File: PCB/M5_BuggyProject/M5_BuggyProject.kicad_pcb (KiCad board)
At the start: 2 copper layers, 9 parts, among them J1 XT60

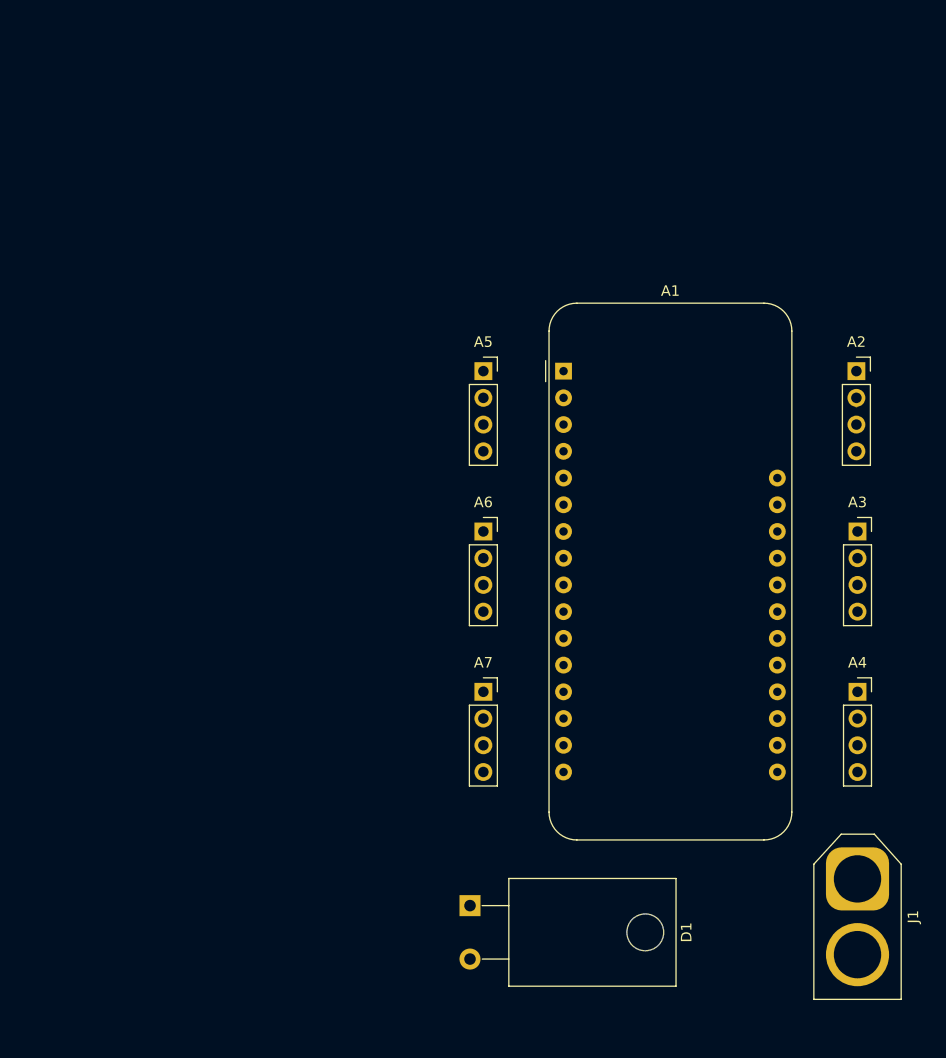
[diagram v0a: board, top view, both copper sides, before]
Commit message: Edited title blocks, netlist
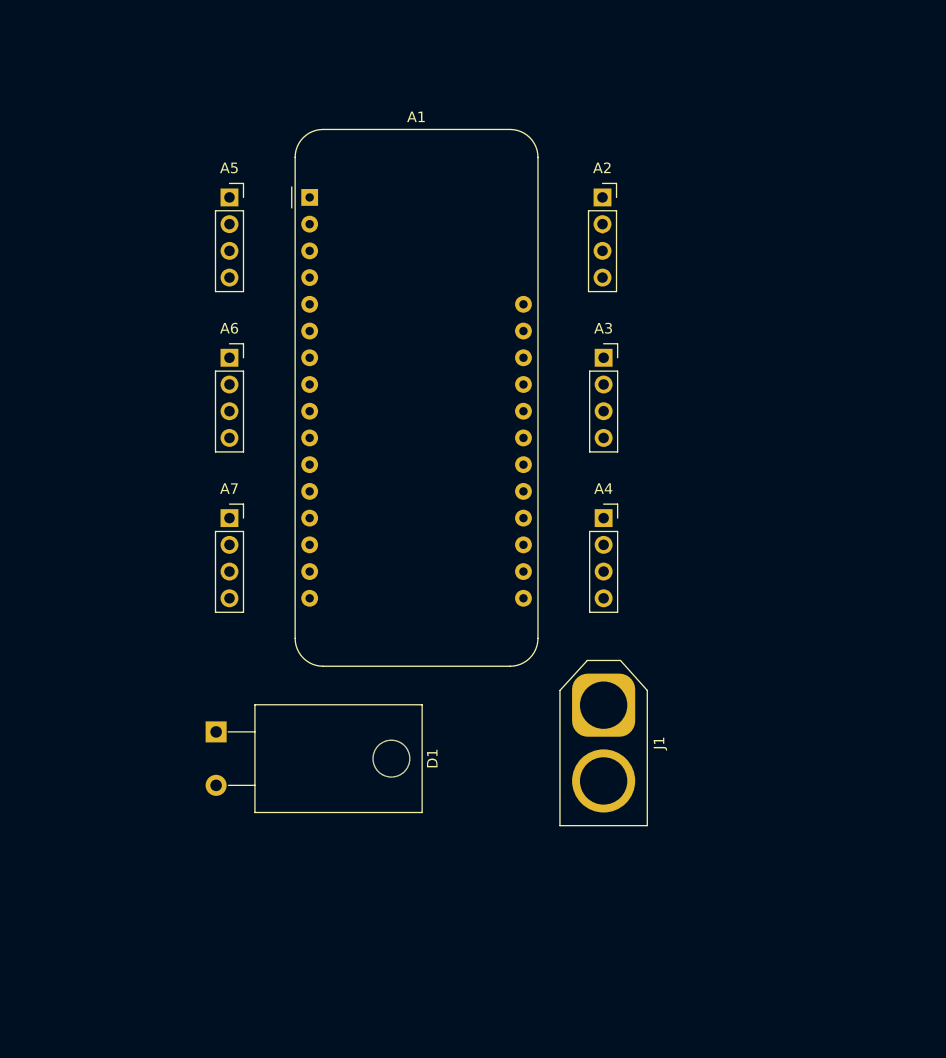
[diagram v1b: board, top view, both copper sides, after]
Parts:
- moved A1 29.2 mm to (101.6, 47.0)
- moved A4 29.2 mm to (129.5, 77.5)
- moved A7 29.2 mm to (94.0, 77.5)
- moved D1 29.2 mm to (92.7, 97.8)
- moved J1 29.2 mm to (129.5, 95.2)
- moved A2 29.2 mm to (129.4, 47.0)
- moved A3 29.2 mm to (129.5, 62.2)
- moved A5 29.2 mm to (94.0, 47.0)
- moved A6 29.2 mm to (94.0, 62.2)
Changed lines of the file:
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@@
     (nets 31)
   )
-  (page A4)
+  (page User 215.9 177.8)
   (title_block
     (title "All-Terrain Buggy")
@@
     (rev v1.0)
     (company "M5 Makerspace")
-    (comment 3 "CC BY 4.0")
+    (comment 2 creativecommons.org/licenses/by/4.0/)
+    (comment 3 "License: CC BY 4.0")
     (comment 4 "Authors: Akshat Sahay, Sebastian Armstrong")
   )
@@
   )
   (module Connector_PinSocket_2.54mm:PinSocket_1x04_P2.54mm_Vertical (layer F.Cu)
-    (at 153.67 93.98)
+    (at 129.54 77.47)
     (descr "Through hole straight socket strip, 1x04, 2.54mm pitch, single row (from Kicad 4.0.7), script generated")
     (tags "Through hole socket strip THT 1x04 2.54mm single row")
@@
   )
   (module Module:Adafruit_Feather (layer F.Cu)
-    (at 125.73 63.5)
+    (at 101.6 46.99)
     (descr "Common footprint for the Adafruit Feather series of boards, https://learn.adafruit.com/adafruit-feather/feather-specification")
     (tags "Adafruit Feather")
@@
   )
   (module Connector_PinSocket_2.54mm:PinSocket_1x04_P2.54mm_Vertical (layer F.Cu)
-    (at 153.565001 63.5)
+    (at 129.435001 46.99)
     (descr "Through hole straight socket strip, 1x04, 2.54mm pitch, single row (from Kicad 4.0.7), script generated")
     (tags "Through hole socket strip THT 1x04 2.54mm single row")
@@
   )
   (module Connector_PinSocket_2.54mm:PinSocket_1x04_P2.54mm_Vertical (layer F.Cu)
-    (at 153.67 78.74)
+    (at 129.54 62.23)
     (descr "Through hole straight socket strip, 1x04, 2.54mm pitch, single row (from Kicad 4.0.7), script generated")
     (tags "Through hole socket strip THT 1x04 2.54mm single row")
@@
   )
   (module Connector_PinSocket_2.54mm:PinSocket_1x04_P2.54mm_Vertical (layer F.Cu)
-    (at 118.11 63.5)
+    (at 93.98 46.99)
     (descr "Through hole straight socket strip, 1x04, 2.54mm pitch, single row (from Kicad 4.0.7), script generated")
     (tags "Through hole socket strip THT 1x04 2.54mm single row")
@@
   )
   (module Connector_PinSocket_2.54mm:PinSocket_1x04_P2.54mm_Vertical (layer F.Cu)
-    (at 118.11 78.74)
+    (at 93.98 62.23)
     (descr "Through hole straight socket strip, 1x04, 2.54mm pitch, single row (from Kicad 4.0.7), script generated")
     (tags "Through hole socket strip THT 1x04 2.54mm single row")
@@
   )
   (module Connector_PinSocket_2.54mm:PinSocket_1x04_P2.54mm_Vertical (layer F.Cu)
-    (at 118.11 93.98)
+    (at 93.98 77.47)
     (descr "Through hole straight socket strip, 1x04, 2.54mm pitch, single row (from Kicad 4.0.7), script generated")
     (tags "Through hole socket strip THT 1x04 2.54mm single row")
@@
   )
   (module Package_TO_SOT_THT:TO-220-2_Horizontal_TabDown (layer F.Cu)
-    (at 116.84 114.3 270)
+    (at 92.71 97.79 270)
     (descr "TO-220-2, Horizontal, RM 5.08mm, see https://www.centralsemi.com/PDFS/CASE/TO-220-2PD.PDF")
     (tags "TO-220-2 Horizontal RM 5.08mm")
@@
   )
   (module Connector_AMASS:AMASS_XT60-F_1x02_P7.20mm_Vertical (layer F.Cu)
-    (at 153.67 111.76 270)
+    (at 129.54 95.25 270)
     (descr "AMASS female XT60, through hole, vertical, https://www.tme.eu/Document/2d152ced3b7a446066e6c419d84bb460/XT60%20SPEC.pdf")
     (tags "XT60 female vertical")
@@
     )
   )
-  (segment (start 153.565001 66.840998) (end 153.565001 66.04) (width 0.25) (layer F.Cu) (net 25))
+  (segment (start 129.435001 50.330998) (end 129.435001 49.53) (width 0.25) (layer F.Cu) (net 25))
 )

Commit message: Added labels, traces for controls
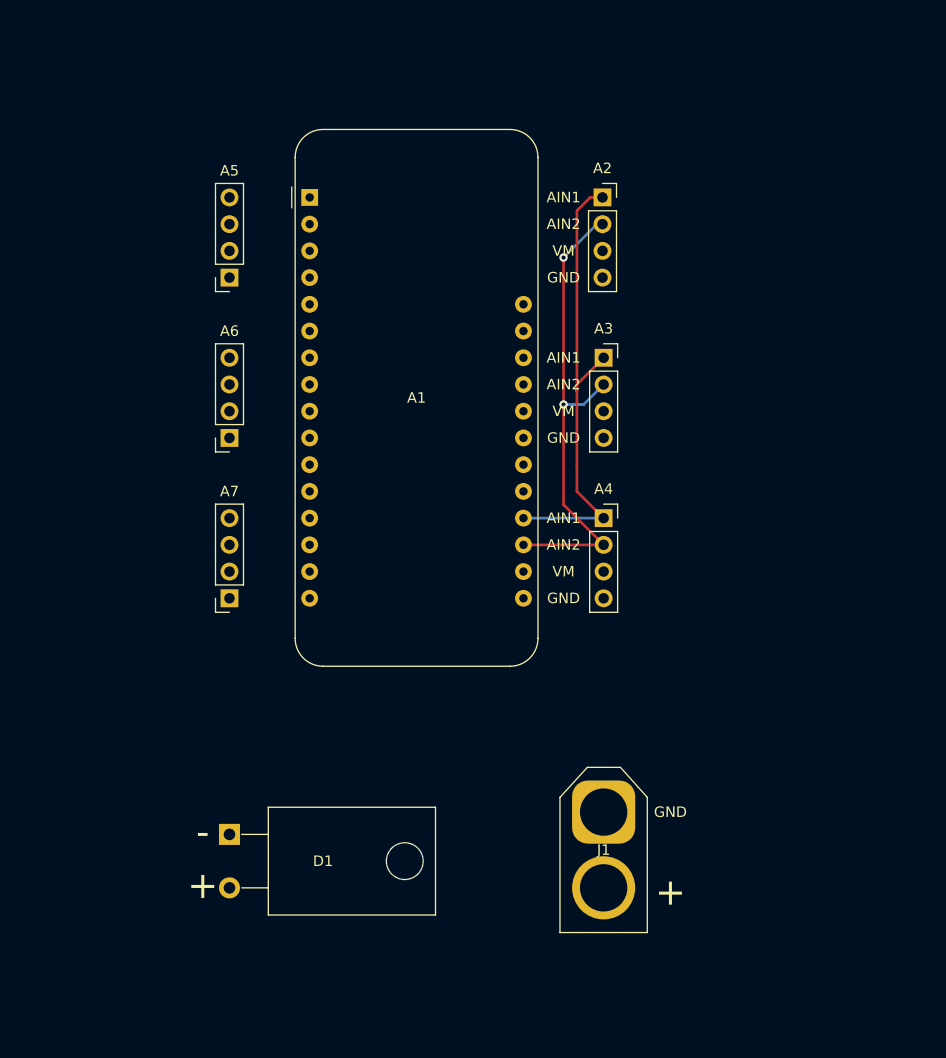
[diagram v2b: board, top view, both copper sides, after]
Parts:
- moved J1 10.2 mm to (129.5, 105.4)
- moved D1 9.82 mm to (94.0, 107.5)
- moved A7 7.62 mm to (94.0, 85.1), turned to 180 degrees
- moved A5 7.62 mm to (94.0, 54.6), turned to 180 degrees
- moved A6 7.62 mm to (94.0, 69.8), turned to 180 degrees
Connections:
- A1 pad 19: AIN1 -> AIN2
- A1 pad 20: AIN2 -> AIN1
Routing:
- net AIN2: track 0.80 -> 46.9 mm, vias 0 -> 2
- net AIN1: track 0.00 -> 45.7 mm
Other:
- net class Default: trace_width 0.25 -> 0.254
- board text added: "+"
- board text added: "-"
- board text added: "AIN1"
- board text added: "AIN2"
- board text added: "GND"
- board text added: "VM"

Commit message: Updated PCB, added Digikey footprint library
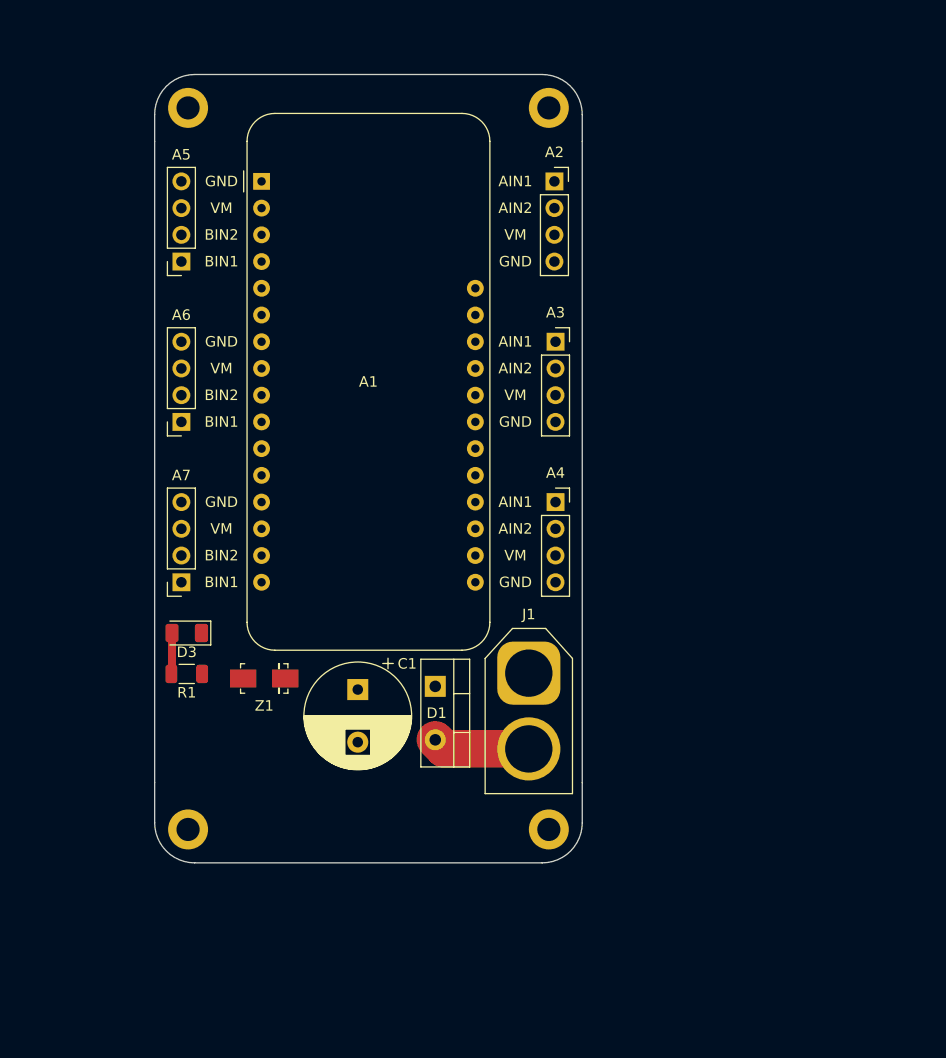
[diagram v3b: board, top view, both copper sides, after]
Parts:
- added C1: 2200uF, Capacitor_THT:CP_Radial_D10.0mm_P5.00mm, F.Cu at (106.2, 93.8)
- added D3: LED, LED_SMD:LED_1206_3216Metric, F.Cu at (89.9, 88.4)
- added M3: MountingHole_2.2mm_M2_DIN965_Pad, MountingHole:MountingHole_2.2mm_M2_DIN965_Pad, F.Cu at (90.0, 107.1)
- added M4: MountingHole_2.2mm_M2_DIN965_Pad, MountingHole:MountingHole_2.2mm_M2_DIN965_Pad, F.Cu at (124.3, 107.1)
- added R1: 698, Resistor_SMD:R_1206_3216Metric, F.Cu at (89.9, 92.3)
- added REF**: MountingHole_2.2mm_M2_DIN965_Pad, MountingHole:MountingHole_2.2mm_M2_DIN965_Pad, F.Cu at (124.3, 38.5)
- added REF**: MountingHole_2.2mm_M2_DIN965_Pad, MountingHole:MountingHole_2.2mm_M2_DIN965_Pad, F.Cu at (90.0, 38.5)
- added Z1: Diode, digikey-footprints:DO-214AC, F.Cu at (97.3, 92.7)
- D1: footprint Package_TO_SOT_THT:TO-220-2_Horizontal_TabDown -> Package_TO_SOT_THT:TO-220-2_Vertical
- J1: footprint Connector_AMASS:AMASS_XT60-F_1x02_P7.20mm_Vertical -> Connector_AMASS:AMASS_XT60-M_1x02_P7.20mm_Vertical
- moved D1 24.1 mm to (113.5, 93.5)
- moved J1 15.0 mm to (122.4, 92.2)
- moved A2 4.82 mm to (124.9, 45.5)
- moved A5 4.82 mm to (89.4, 53.1)
- moved A6 4.82 mm to (89.4, 68.3)
- moved A7 4.82 mm to (89.4, 83.6)
- moved A1 4.82 mm to (97.0, 45.5)
- moved A4 4.82 mm to (125.0, 75.9)
- moved A3 4.82 mm to (125.0, 60.7)
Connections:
- net +7.5V renamed +12V
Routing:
- net AIN2: track 46.9 -> 0.53 mm, vias 2 -> 0
- net AIN1: track 45.7 -> 0.63 mm
- net VCC: track 0.00 -> 9.25 mm
- net Net-(D3-Pad2): track 0.00 -> 3.91 mm
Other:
- board outline added: 40.6 x 74.9 mm
- board text added: "BIN1"
- board text added: "BIN2"
- board text removed: "+"
- board text removed: "-"

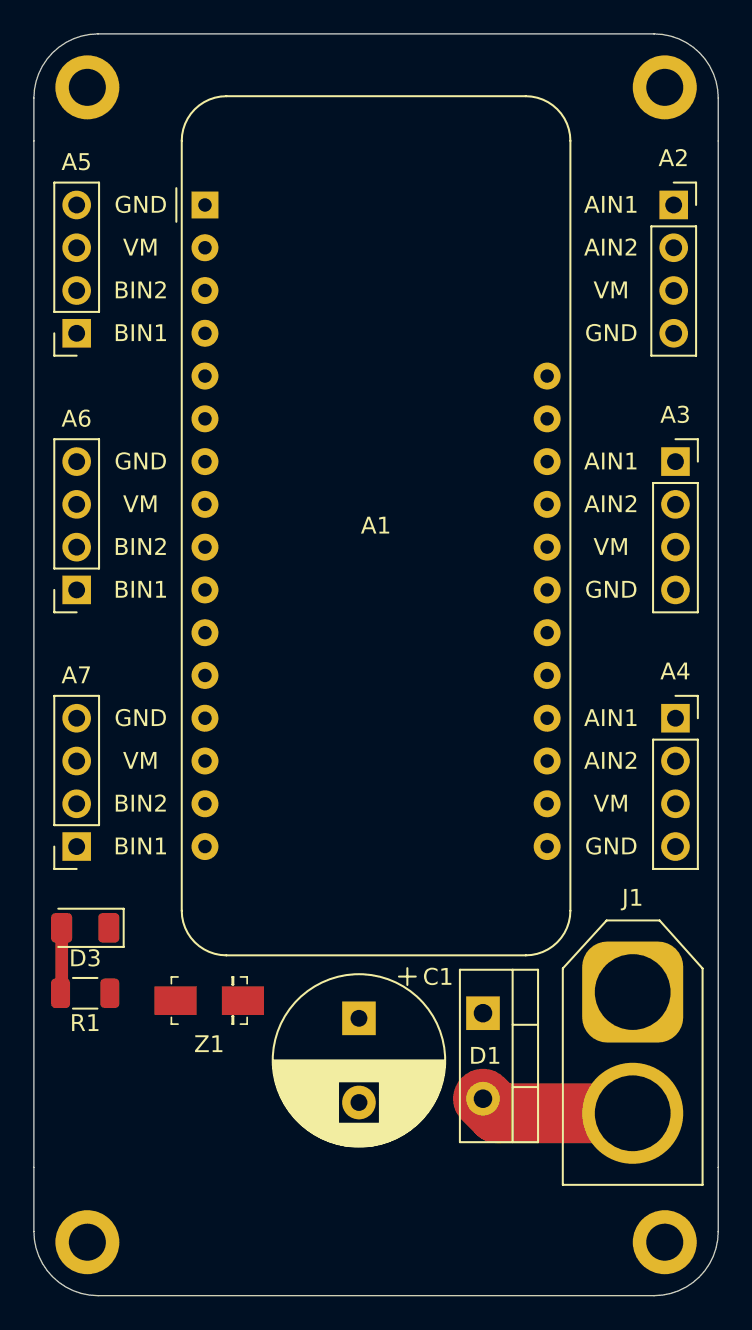
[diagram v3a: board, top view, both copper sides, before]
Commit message: Added graphics to PCB
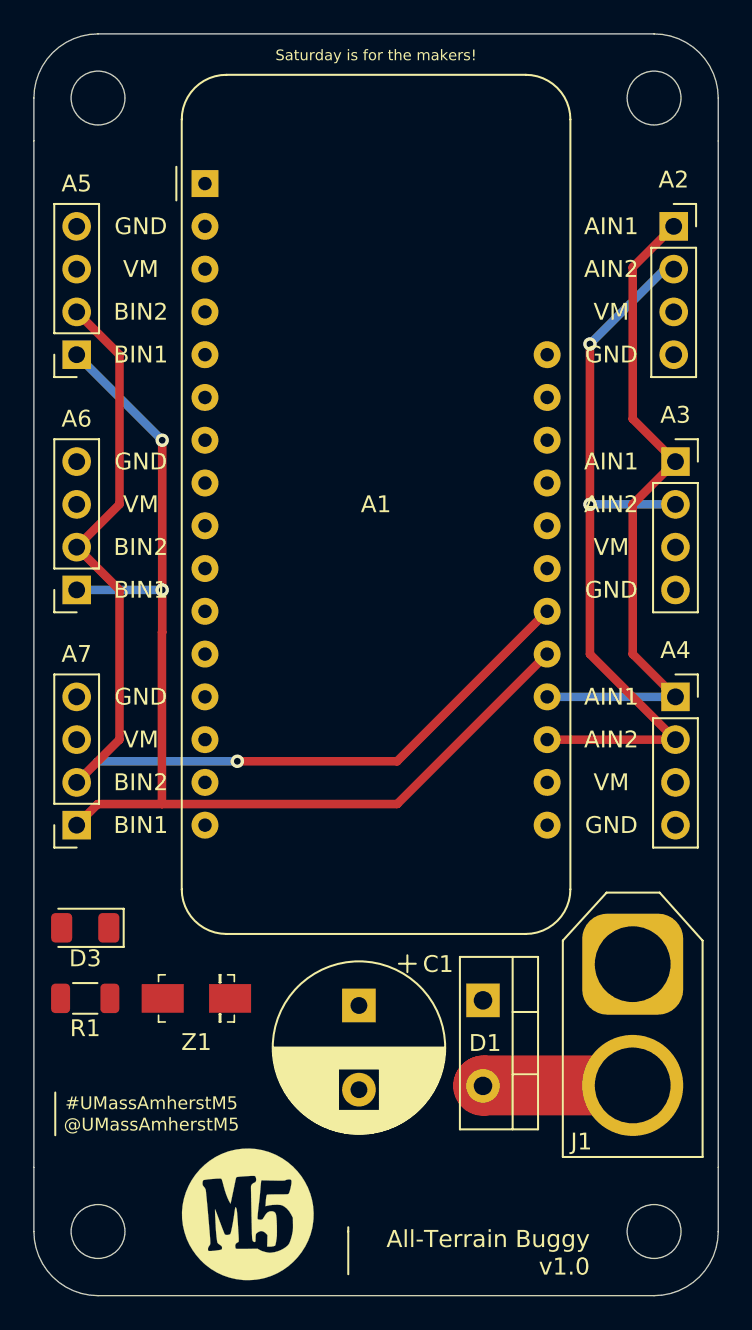
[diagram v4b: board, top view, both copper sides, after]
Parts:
- removed M3, M4: MountingHole_2.2mm_M2_DIN965_Pad, MountingHole:MountingHole_2.2mm_M2_DIN965_Pad
- removed the REF** at (124.3, 38.5)
- removed the REF** at (90.0, 38.5)
- added G***: LOGO, Figures:M5_logo, F.Cu at (99.6, 105.4)
- added REF**: MountingHole_3.2mm_M3, MountingHole:MountingHole_3.2mm_M3, F.Cu at (123.7, 39.1)
- added REF**: MountingHole_3.2mm_M3, MountingHole:MountingHole_3.2mm_M3, F.Cu at (90.7, 39.1)
- added REF**: MountingHole_3.2mm_M3, MountingHole:MountingHole_3.2mm_M3, F.Cu at (123.7, 106.4)
- added REF**: MountingHole_3.2mm_M3, MountingHole:MountingHole_3.2mm_M3, F.Cu at (90.7, 106.4)
- moved J1 1.66 mm to (122.4, 90.6)
- moved A1 1.27 mm to (97.0, 44.2)
- moved A5 1.27 mm to (89.4, 54.4)
- moved A2 1.27 mm to (124.9, 46.7)
- moved A4 1.27 mm to (125.0, 74.7)
- moved A7 1.27 mm to (89.4, 82.3)
- moved Z1 0.77 mm to (96.5, 92.6)
- moved C1 0.76 mm to (106.2, 93.0)
- moved D1 0.76 mm to (113.5, 92.7)
- moved R1 0.30 mm to (89.9, 92.6)
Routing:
- net BIN1: track 0.00 -> 66.0 mm, vias 0 -> 2
- net BIN2: track 0.25 -> 64.3 mm, vias 0 -> 1
- net AIN2: track 0.53 -> 45.1 mm, vias 0 -> 2
- net AIN1: track 0.63 -> 39.7 mm
- net Net-(D3-Pad2): track 3.91 -> 0.00 mm
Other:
- board text added: "#UMassAmherstM5"
- board text added: "@UMassAmherstM5"
- board text added: "All-Terrain Buggy v1.0"
- board text added: "Saturday is for the makers!"

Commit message: Finalised PCB for v1.0
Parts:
- removed REF** (x4): MountingHole_3.2mm_M3, MountingHole:MountingHole_3.2mm_M3
- added BZ1: BEEP, Buzzer_Beeper:Buzzer_12x9.5RM7.6, F.Cu at (107.2, 44.2)
- added D2: ORANGE, LED_SMD:LED_1206_3216Metric, F.Cu at (89.4, 45.5)
- added D4: ORANGE, LED_SMD:LED_1206_3216Metric, F.Cu at (93.2, 45.5)
- added H1: M, MountingHole:MountingHole_3.2mm_M3_Pad_Via, F.Cu at (80.5, 39.1)
- added H2: M, MountingHole:MountingHole_3.2mm_M3_Pad_Via, F.Cu at (113.5, 39.1)
- added H3: M, MountingHole:MountingHole_3.2mm_M3_Pad_Via, F.Cu at (113.5, 121.7)
- added H4: M, MountingHole:MountingHole_3.2mm_M3_Pad_Via, F.Cu at (80.5, 121.7)
- added J2: VCC, TestPoint:TestPoint_Loop_D1.80mm_Drill1.0mm_Beaded, F.Cu at (103.4, 117.9)
- added J3: 10V, TestPoint:TestPoint_Loop_D1.80mm_Drill1.0mm_Beaded, F.Cu at (98.3, 117.8)
- added R2: 100, Resistor_SMD:R_1206_3216Metric, F.Cu at (89.4, 40.4)
- added R3: 100, Resistor_SMD:R_1206_3216Metric, F.Cu at (93.2, 40.4)
- D3: value LED -> BLUE
- R1: value 698 -> 330
- moved G*** 18.5 mm to (89.4, 120.9)
- moved Z1 18.4 mm to (84.3, 106.4), turned to 90 degrees
- moved R1 18.1 mm to (79.9, 107.6), turned to 270 degrees
- moved D1 18.0 mm to (103.4, 107.6)
- moved J1 18.0 mm to (112.3, 105.4)
- moved C1 17.5 mm to (95.9, 107.2)
- moved A1 17.3 mm to (86.9, 58.2)
- moved A4 17.3 mm to (114.8, 88.6)
- moved A7 17.3 mm to (79.2, 96.3)
- moved D3 16.4 mm to (79.9, 101.3), turned to 270 degrees
- moved A6 12.7 mm to (79.2, 75.9)
- moved A3 12.7 mm to (114.8, 68.3)
- moved A2 10.2 mm to (114.7, 48.0)
- moved A5 10.2 mm to (79.2, 55.6)
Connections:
- net +12V renamed +10V
- net Net-(A1-Pad8) renamed CHANNEL_3
- A1 pad 10: Net-(A1-Pad10) -> CONFIG_R
- A1 pad 24: Net-(A1-Pad24) -> BEEP
- A1 pad 9: Net-(A1-Pad9) -> CONFIG_L
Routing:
- net CONFIG_R: track 0.00 -> 36.8 mm
- net BEEP: track 0.00 -> 36.4 mm
- net CONFIG_L: track 0.00 -> 32.7 mm
- net BIN2: track 64.3 -> 77.0 mm
- net AIN1: track 39.7 -> 52.4 mm
- net BIN1: track 66.0 -> 78.7 mm
- net AIN2: track 45.1 -> 57.5 mm
- net +10V: track 0.00 -> 11.1 mm, vias 0 -> 1
- net VCC: track 8.90 -> 14.1 mm
- net Net-(D3-Pad2): track 0.00 -> 3.44 mm
- net Net-(D4-Pad1): track 0.00 -> 2.22 mm
- net Net-(D2-Pad1): track 0.00 -> 2.22 mm
- added copper zone on B.Cu, net +10V
- added copper zone on F.Cu, net GND
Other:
- board size 40.6 x 74.9 mm -> 40.6 x 90.2 mm
- board text added: "+"
- board text added: "-"
- board text added: "10V"
- board text added: "CON_L"
- board text added: "CON_R"
- board text added: "Designers: Akshat Sahay 2023, Sebastian Armstrong 2024 License: CC BY 4.0"
- board text added: "VCC"

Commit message: Added gerber files
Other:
- board text added: "JLCJLCJLCJLC"
- board text added: "umassamherstm5.org"

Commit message: Added social logos
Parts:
- added G***: LOGO, Figures:Instagram_logo, F.Cu at (79.0, 113.3)
- moved R1 3.76 mm to (79.9, 103.9), turned to 180 degrees
- moved Z1 2.54 mm to (86.9, 106.4), turned to 0 degrees
- moved G*** 1.27 mm to (89.4, 119.6)
- turned D3 to 0 degrees
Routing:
- net Net-(D3-Pad2): track 3.44 -> 2.57 mm
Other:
- board text added: "BEEP"
